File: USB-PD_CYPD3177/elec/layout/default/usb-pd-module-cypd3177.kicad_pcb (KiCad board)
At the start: 2 copper layers, 40 x 40 mm, 72 parts

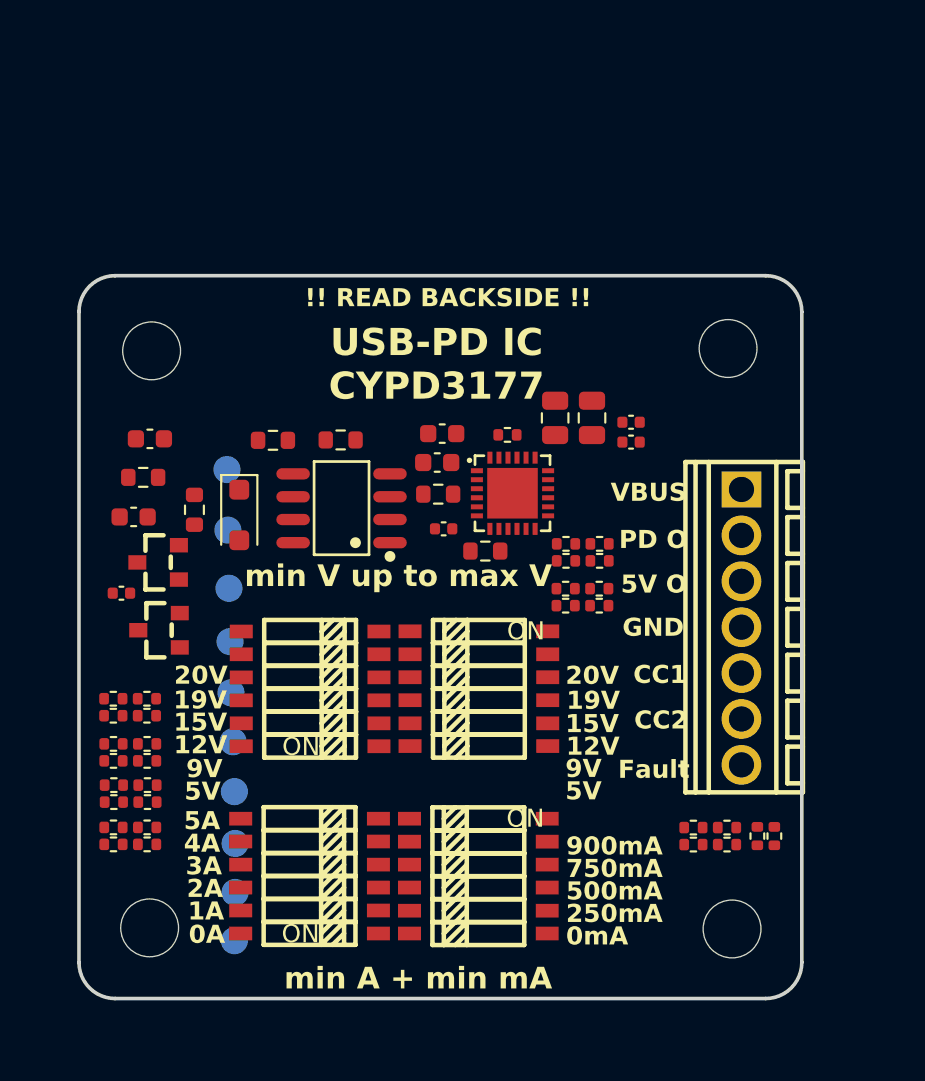
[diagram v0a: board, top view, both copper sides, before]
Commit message: fixed 3d model positions and links
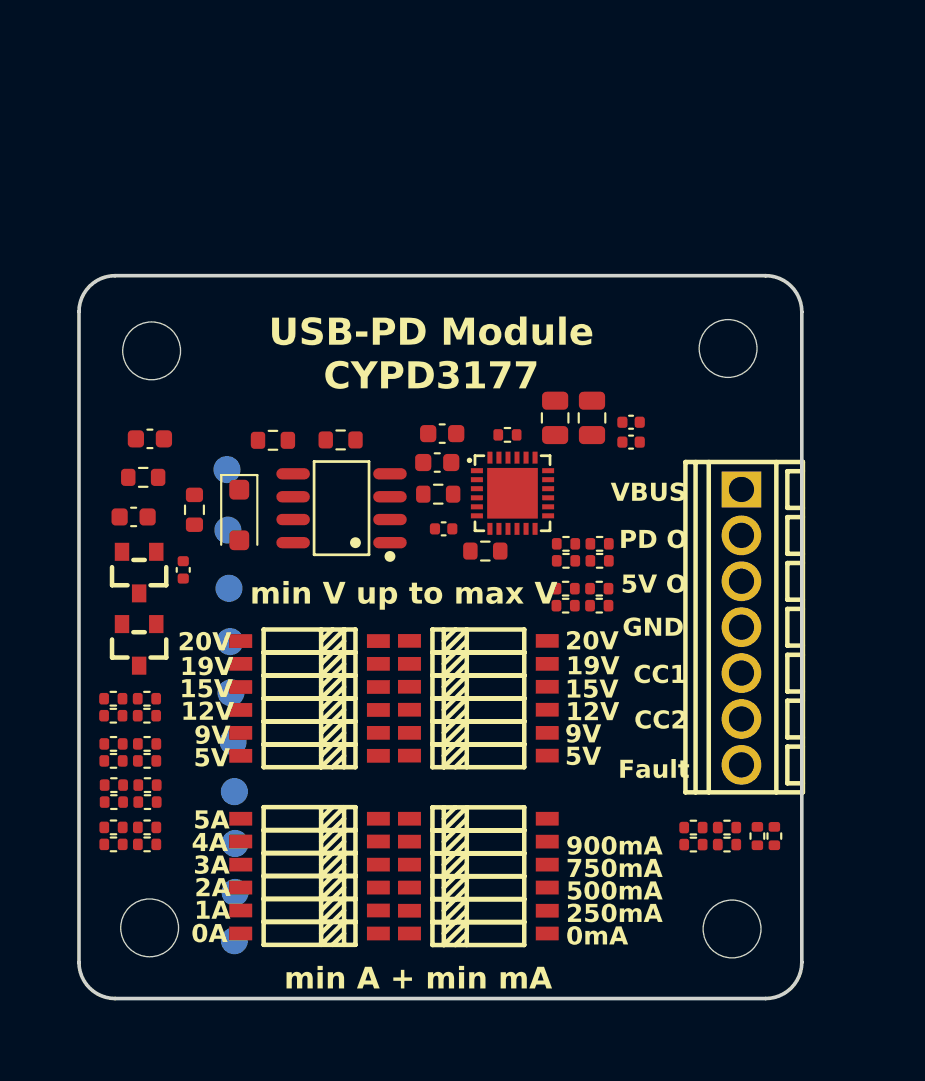
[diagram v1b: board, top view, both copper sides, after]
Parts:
- C1, C6: value 3.3 +/- 0.33 (10%) microfarad -> 3.3uF +/- 10%
- C10, C9: value 100 +/- 10 (10%) nanofarad -> 0.1uF +/- 10%
- C2, C3, C7, C8: value 1000 +/- 100 (10%) nanofarad -> 1uF +/- 10%
- C4: value 390 +/- 19.5 (5%) picofarad -> 390pF +/- 5%
- R1, R15, R23, R31: value 10 +/- 0.1 (1%) kiloohm -> 10kohm +/- 1%
- R10, R12, R13, R14, R16, R18, R20, R21, R22, R24, R26, R28, R29, R30, R32, R34, R36, R37, R8: value 5.1 +/- 0.05 (1%) kiloohm -> 5.1kohm +/- 1%
- R11, R19, R27, R35: value 2.4 +/- 0.02 (1%) kiloohm -> 2.4kohm +/- 1%
- R17, R2, R25, R33, R5, R9: value 1000 +/- 10 (1%) ohm -> 1kohm +/- 1%
- R3, R4: value 49.9 +/- 0.5 (1%) kiloohm -> 49.9kohm +/- 1%
- R6: value 100 +/- 5 (5%) kiloohm -> 100kohm +/- 5%
- R7: value 2 +/- 0.02 (1%) kiloohm -> 2kohm +/- 1%
- moved C9 3.66 mm to (155.1, 93.0), turned to 90 degrees
- moved U3 1.37 mm to (152.7, 97.1), turned to 90 degrees
- moved U4 1.19 mm to (152.7, 93.1), turned to 90 degrees
- moved U5 0.53 mm to (162.1, 100.1)
- moved U6 0.53 mm to (171.5, 100.1)
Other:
- board text added: "How to use: Make sure that for min V, max V, min A, min mA you have for each exactly ONE selection always turned ON."
- board text added: "USB-PD Module CYPD3177"
- board text removed: "!! READ BACKSIDE !!"
- board text removed: "How to use: Make sure that for min V, max V, min A,min mA you have for each exactly ONE selection always turned ON."
- board text removed: "USB-PD IC CYPD3177"

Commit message: finished dev module for USB PD pcb layout
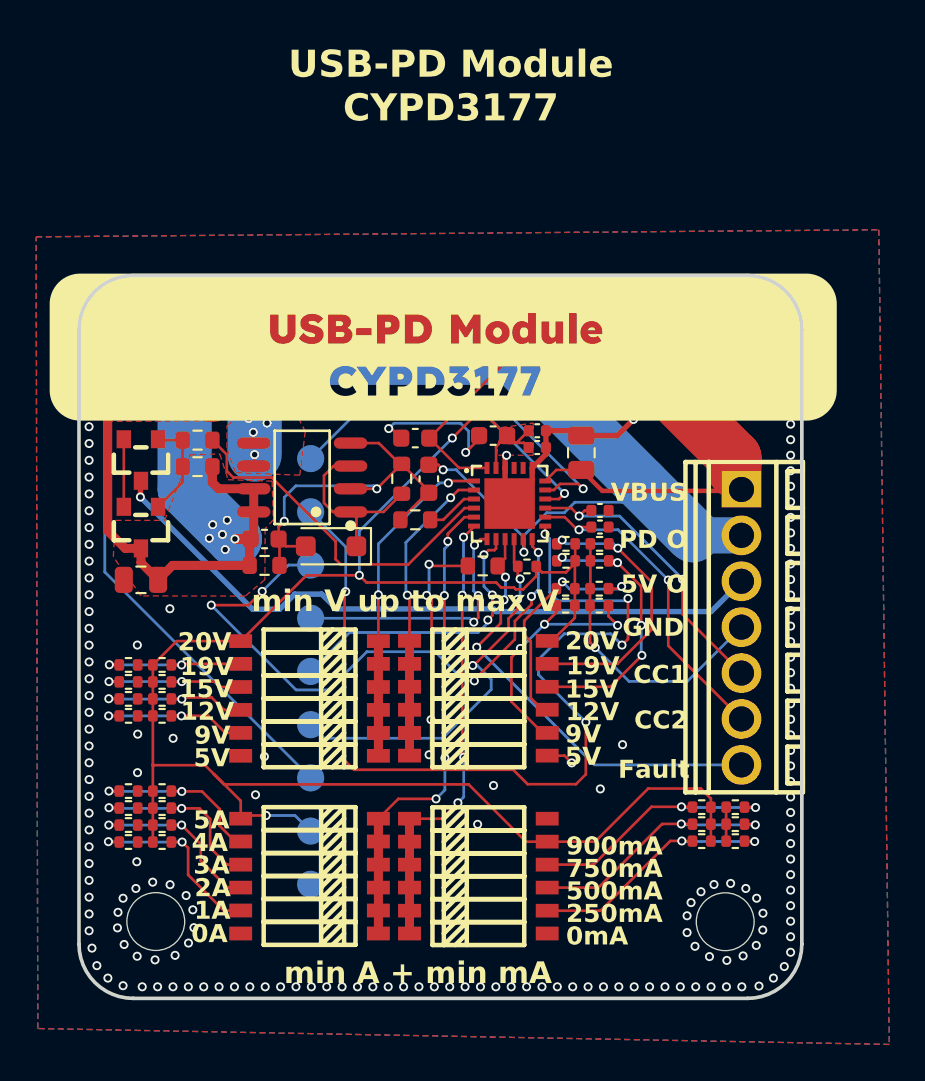
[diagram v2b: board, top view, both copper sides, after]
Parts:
- moved C1 24.6 mm to (152.8, 93.5), turned to 180 degrees
- moved U11 21.8 mm to (162.2, 83.9)
- moved C9 21.0 mm to (174.7, 85.3), turned to 0 degrees
- moved C8 19.0 mm to (172.3, 85.5), turned to 180 degrees
- moved C7 16.2 mm to (168.0, 85.7), turned to 180 degrees
- moved U18 12.9 mm to (162.2, 98.6)
- moved U19 12.7 mm to (162.2, 101.5)
- moved C2 10.5 mm to (159.6, 91.3)
- moved U10 8.98 mm to (162.2, 110.4)
- moved U13 8.83 mm to (162.2, 107.4)
- moved R7 7.36 mm to (174.2, 92.8)
- moved C10 6.86 mm to (174.7, 86.2)
- moved U3 6.49 mm to (152.8, 90.6)
- moved U4 6.23 mm to (152.8, 86.9)
- moved C5 6.05 mm to (178.2, 90.6), turned to 0 degrees
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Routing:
- net vcc-3: track 0.00 -> 105.4 mm, vias 0 -> 3
- net vcc: track 0.00 -> 85.5 mm, vias 0 -> 11
- net vcc-4: track 0.00 -> 71.4 mm, vias 0 -> 1
- net vcc-1: track 0.00 -> 54.5 mm, vias 0 -> 8
- net gnd: track 0.00 -> 53.4 mm, vias 0 -> 239
- net hpi_scl: track 0.00 -> 52.7 mm, vias 0 -> 5
- net vcc-2: track 0.00 -> 38.2 mm, vias 0 -> 1
- net hpi_sda: track 0.00 -> 33.9 mm, vias 0 -> 5
- net isnk_coarse: track 0.00 -> 26.8 mm, vias 0 -> 4
- net isnk_fine: track 0.00 -> 25.1 mm, vias 0 -> 4
- net fault: track 0.00 -> 24.3 mm, vias 0 -> 3
- net power_out_vbus_load_switch.load_switch_mosfet-gnd: track 0.00 -> 22.2 mm, vias 0 -> 2
- net flip: track 0.00 -> 21.6 mm, vias 0 -> 3
- net safe_pwr_en: track 0.00 -> 19.7 mm
- net dplus: track 0.00 -> 19.6 mm, vias 0 -> 1
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- added copper zone on B.Cu, net gnd
- added copper zone on F.Cu, net gnd
- added copper zone on F.Cu, net vcc
- added copper zone on F.Cu, net vcc-1
- added copper zone on F.Cu, net vcc-3
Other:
- outline, holes or cut-outs redrawn
- board text added: "D+"
- board text added: "IC 1.8V"
- board text added: "IC 3.3V"
- board text added: "bit.ly/3WI7WtW"
- board text removed: "ISNK FINE"
- board text removed: "VBUS MAX"
- board text removed: "VBUS MIN"
- board text removed: "bit.ly/xxxxx"

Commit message: added designed by glowingkitty
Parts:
- moved REF** 29.9 mm to (168.4, 108.7)
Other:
- board text added: "designed by glowingkitty"
